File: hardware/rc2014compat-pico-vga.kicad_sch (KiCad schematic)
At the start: 50 parts, among them J1 Conn_01x10_Female, J2 DB15_Female_HighDensity_Mount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, J3 USB_C_Receptacle_USB2.0, J4 RC2014-ENH, J5 RC2014-STD, SW1 C319395, SW2 C319395, SW3 C319395, SW4 C319395, SW5 SW_DPDT_x2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

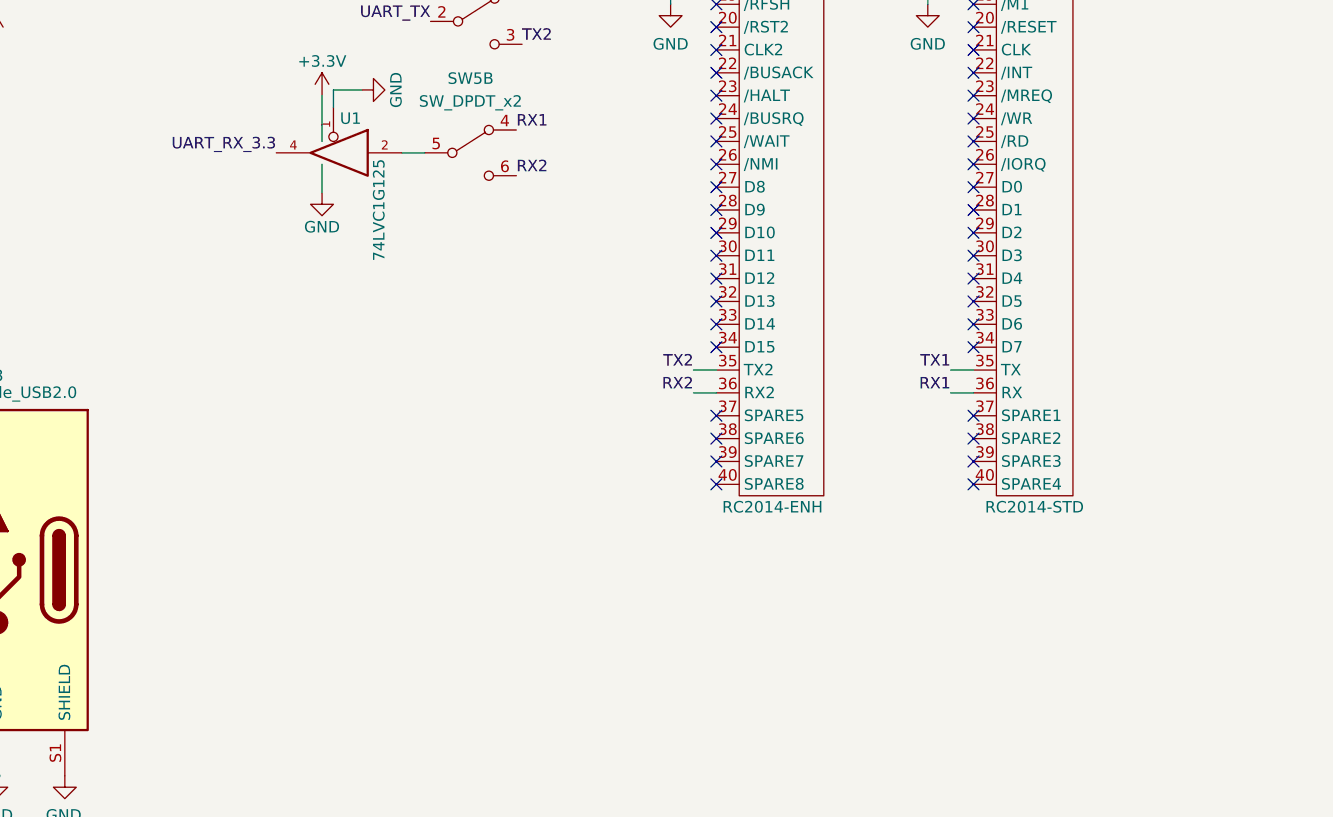
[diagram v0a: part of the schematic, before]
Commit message: hardware: pcb routing complete
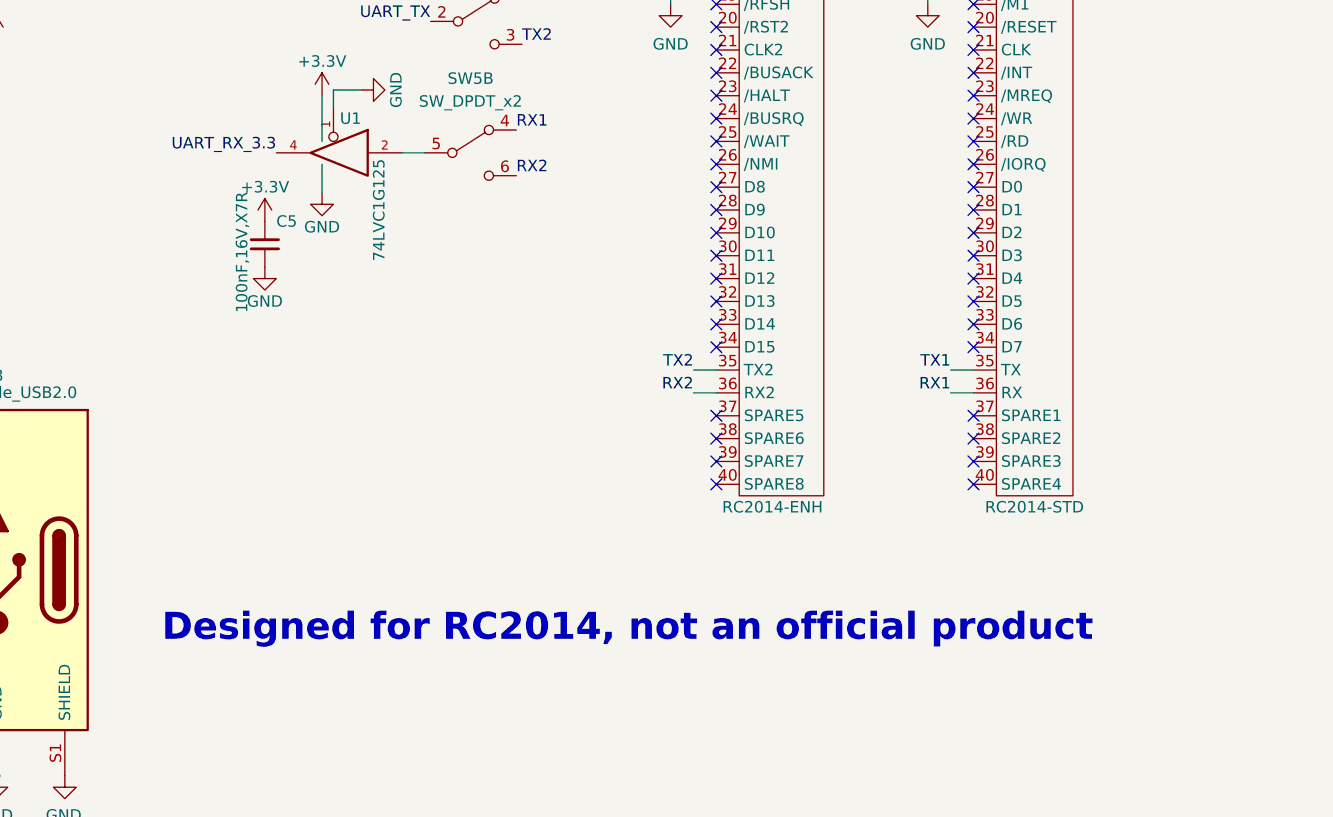
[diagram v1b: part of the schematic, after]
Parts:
- removed R31, R32: 47, R_0603_1608Metric, symbol jlcpcb-basic-resistor-0603:47
- added C5: 100nF,16V,X7R, C_0402_1005Metric, symbol jlcpcb-basic-capacitor-0402:100nF,16V,X7R
- added R31, R32: 47, R_0402_1005Metric, symbol jlcpcb-basic-resistor-0402:47
- J2: footprint (none) -> tom-connectors:DSUB-15-HD_Female_Horizontal_P2.29x1.98mm_EdgePinOffset3.03mm_Housed_MountingHolesOffset4.94mm
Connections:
- net +3.3V: now also C5.1
- net GND: now also C5.2
- net RP2040/GPIO16: now also R31.2
- net RP2040/GPIO17: now also R32.2
- net VGA_HS: now also R31.1
- net VGA_VS: now also R32.1
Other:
- note added: "Designed for RC2014, not an official product"
